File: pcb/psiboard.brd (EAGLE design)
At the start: 102.9 x 22.9 mm, 4 parts

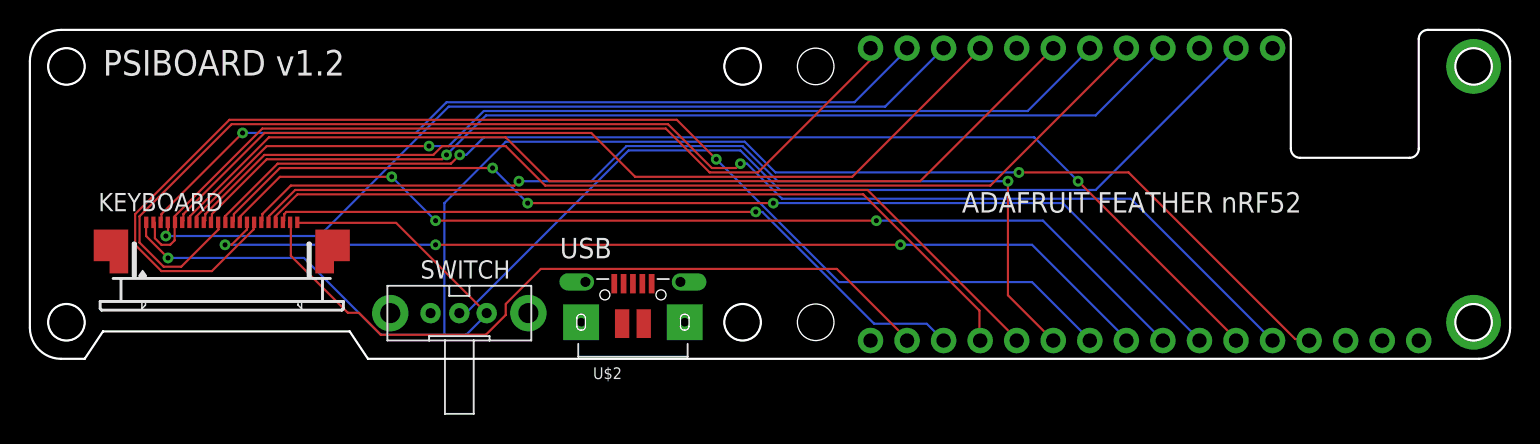
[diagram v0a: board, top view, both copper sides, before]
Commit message: Fix the routing fro the USB.
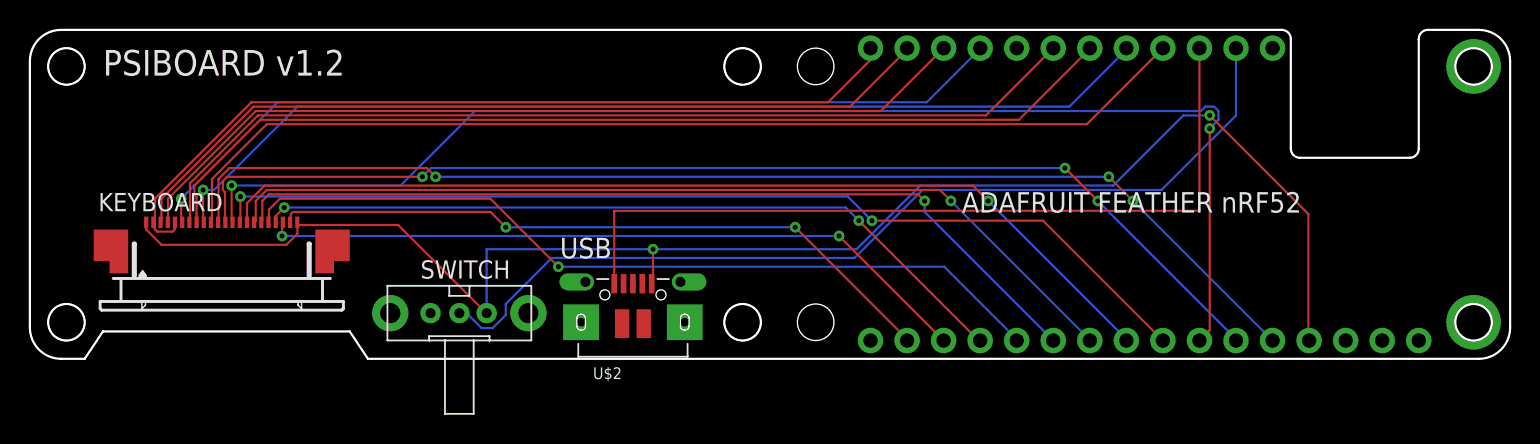
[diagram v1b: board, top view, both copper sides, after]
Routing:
- net USB: track 0.00 -> 57.0 mm
- net 29: track 88.3 -> 64.2 mm
- net 4: track 74.0 -> 90.0 mm, vias 3 -> 2
- net 2: track 97.5 -> 81.5 mm, vias 1 -> 3
- net GND: track 120.7 -> 107.9 mm
- net 12: track 67.8 -> 61.3 mm, vias 2 -> 1
- net 6: track 51.9 -> 47.2 mm, vias 0 -> 2
- net 25: track 60.7 -> 58.8 mm
- net 14: track 55.4 -> 53.5 mm, vias 0 -> 2
- net EN: track 63.9 -> 65.7 mm
- net 30: track 63.3 -> 61.5 mm, vias 0 -> 1
- net 7: track 67.4 -> 68.8 mm, vias 1 -> 0
- net 16: track 71.5 -> 72.9 mm, vias 1 -> 0
- net 11: track 67.8 -> 66.6 mm
- net 15: track 71.7 -> 70.6 mm, vias 0 -> 1
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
